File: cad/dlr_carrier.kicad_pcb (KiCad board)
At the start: 2 copper layers, 100 x 80 mm, 24 parts, among them J1 5V_IN, J2 CM4, J3 RS485, J4 USB_DEBUG, J5 I2C, J6 SPI, J7 GPIO, Q1 SI2301, U1 MAX3485, U2 CP2102N

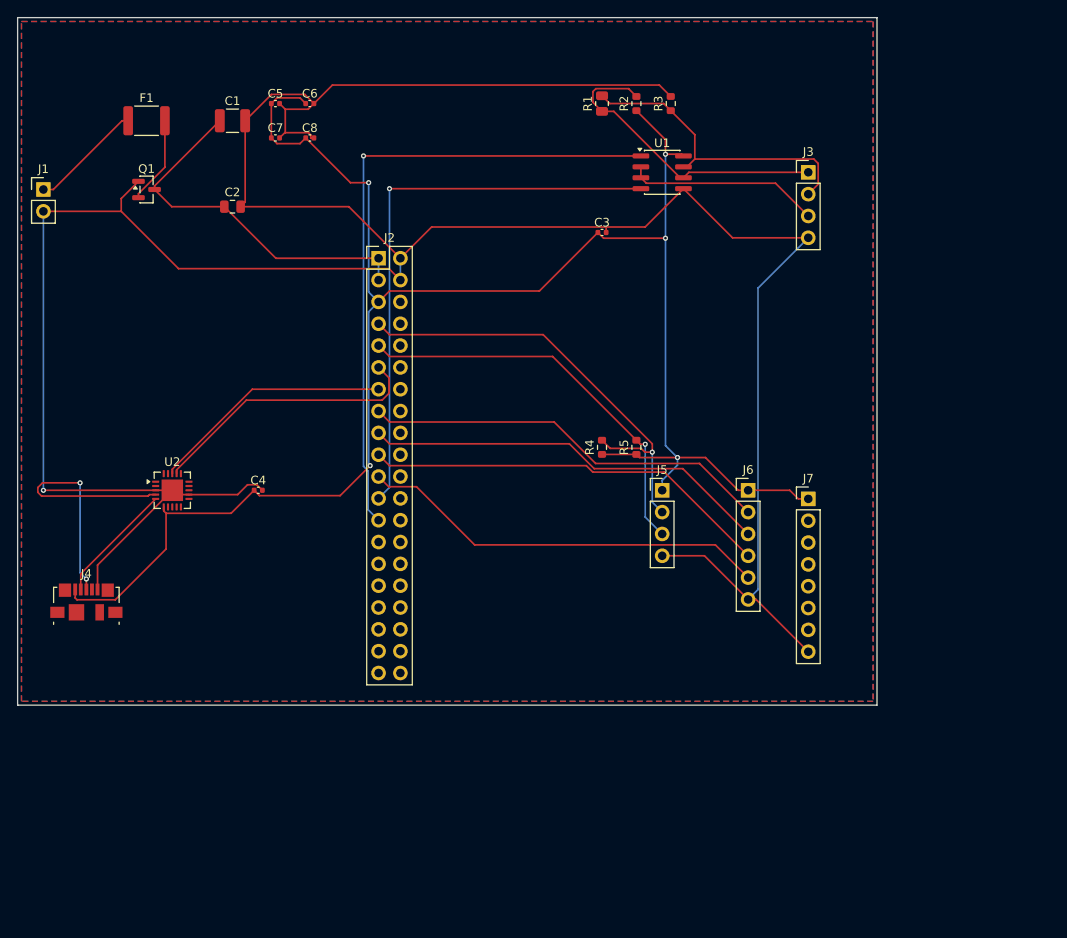
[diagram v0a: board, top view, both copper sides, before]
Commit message: 🔧 chore(cad): regenerate PCB layout, gerbers, and fab artifacts
Co-Authored-By: Claude Opus 4.7 (1M context) <noreply@anthropic.com>
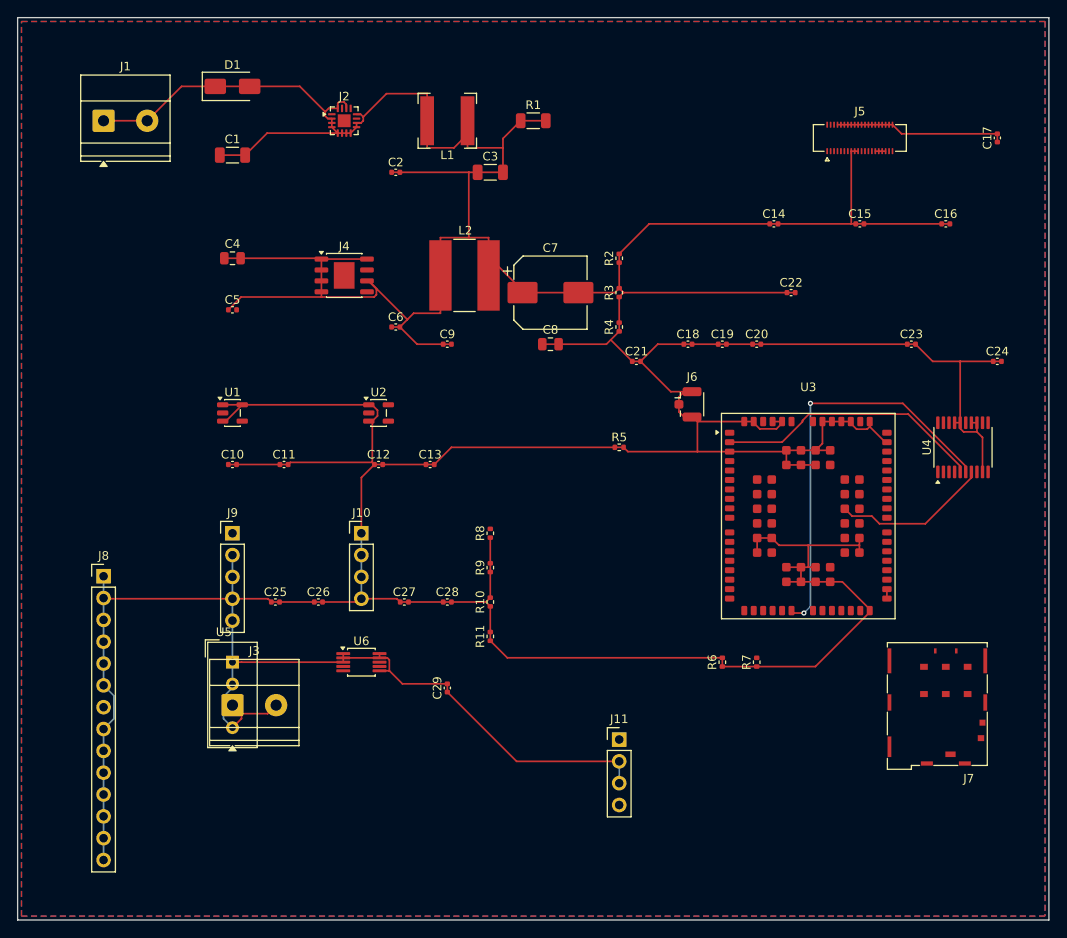
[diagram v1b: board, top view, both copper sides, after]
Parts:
- removed F1: 2A, Fuse:Fuse_1812_4532Metric
- removed Q1: SI2301, Package_TO_SOT_SMD:SOT-23
- added C10: 1uF, Capacitor_SMD:C_0402_1005Metric, F.Cu at (125.0, 132.0)
- added C11: 1uF, Capacitor_SMD:C_0402_1005Metric, F.Cu at (131.0, 132.0)
- added C12: 1uF, Capacitor_SMD:C_0402_1005Metric, F.Cu at (142.0, 132.0)
- added C13: 1uF, Capacitor_SMD:C_0402_1005Metric, F.Cu at (148.0, 132.0)
- added C14: 100nF, Capacitor_SMD:C_0402_1005Metric, F.Cu at (188.0, 104.0)
- added C15: 100nF, Capacitor_SMD:C_0402_1005Metric, F.Cu at (198.0, 104.0)
- added C16: 100nF, Capacitor_SMD:C_0402_1005Metric, F.Cu at (208.0, 104.0)
- added C17: 100nF, Capacitor_SMD:C_0402_1005Metric, F.Cu at (214.0, 94.0)
- added C18: 4.7uF, Capacitor_SMD:C_0402_1005Metric, F.Cu at (178.0, 118.0)
- added C19: 100nF, Capacitor_SMD:C_0402_1005Metric, F.Cu at (182.0, 118.0)
- added C20: 100nF, Capacitor_SMD:C_0402_1005Metric, F.Cu at (186.0, 118.0)
- added C21: DNP, Capacitor_SMD:C_0402_1005Metric, F.Cu at (172.0, 120.0)
- added C22: DNP, Capacitor_SMD:C_0402_1005Metric, F.Cu at (190.0, 112.0)
- added C23: 100nF, Capacitor_SMD:C_0402_1005Metric, F.Cu at (204.0, 118.0)
- added C24: 100nF, Capacitor_SMD:C_0402_1005Metric, F.Cu at (214.0, 120.0)
- added C25: 100nF, Capacitor_SMD:C_0402_1005Metric, F.Cu at (130.0, 148.0)
- added C26: 100nF, Capacitor_SMD:C_0402_1005Metric, F.Cu at (135.0, 148.0)
- added C27: 100nF, Capacitor_SMD:C_0402_1005Metric, F.Cu at (145.0, 148.0)
- added C28: 100nF, Capacitor_SMD:C_0402_1005Metric, F.Cu at (150.0, 148.0)
- added C29: 10nF, Capacitor_SMD:C_0402_1005Metric, F.Cu at (150.0, 158.0)
- added C9: 100nF, Capacitor_SMD:C_0402_1005Metric, F.Cu at (150.0, 118.0)
- added D1: SS34, Diode_SMD:D_SMA, F.Cu at (125.0, 88.0)
- added J10: YL-83, Connector_PinHeader_2.54mm:PinHeader_1x04_P2.54mm_Vertical, F.Cu at (140.0, 140.0)
- added J11: DEBUG_UART, Connector_PinHeader_2.54mm:PinHeader_1x04_P2.54mm_Vertical, F.Cu at (170.0, 164.0)
- added J8: FLIR_LEPTON, Connector_PinHeader_2.54mm:PinHeader_1x14_P2.54mm_Vertical, F.Cu at (110.0, 145.0)
- added J9: SI1145, Connector_PinHeader_2.54mm:PinHeader_1x05_P2.54mm_Vertical, F.Cu at (125.0, 140.0)
- added L1: 6.8uH, Inductor_SMD:L_Bourns-SRN6028, F.Cu at (150.0, 92.0)
- added L2: 10uH, Inductor_SMD:L_Bourns-SRN8040_8x8.15mm, F.Cu at (152.0, 110.0)
- added R10: 2.2k, Resistor_SMD:R_0402_1005Metric, F.Cu at (155.0, 148.0)
- added R11: 2.2k, Resistor_SMD:R_0402_1005Metric, F.Cu at (155.0, 152.0)
- added R6: 100k, Resistor_SMD:R_0402_1005Metric, F.Cu at (182.0, 155.0)
- added R7: 10k, Resistor_SMD:R_0402_1005Metric, F.Cu at (186.0, 155.0)
- added R8: 10k, Resistor_SMD:R_0402_1005Metric, F.Cu at (155.0, 140.0)
- added R9: 10k, Resistor_SMD:R_0402_1005Metric, F.Cu at (155.0, 144.0)
- added U3: BG770A-NA, RF_GSM:Quectel_BG95, F.Cu at (192.0, 138.0)
- added U4: TXS0108E, Package_SO:TSSOP-20_4.4x6.5mm_P0.65mm, F.Cu at (210.0, 130.0)
- added U5: DHT22, Sensor:Aosong_DHT11_5.5x12.0_P2.54mm, F.Cu at (125.0, 155.0)
- added U6: ADS1115, Package_SO:MSOP-10_3x3mm_P0.5mm, F.Cu at (140.0, 155.0)
- C1: value 100uF -> 22uF; footprint Capacitor_SMD:C_1210_3225Metric -> Capacitor_SMD:C_1206_3216Metric
- C2: value 10uF -> 100nF; footprint Capacitor_SMD:C_0805_2012Metric -> Capacitor_SMD:C_0402_1005Metric
- C3: value 100nF -> 22uF; footprint Capacitor_SMD:C_0402_1005Metric -> Capacitor_SMD:C_1206_3216Metric
- C4: value 100nF -> 4.7uF; footprint Capacitor_SMD:C_0402_1005Metric -> Capacitor_SMD:C_0805_2012Metric
- C7: value 100nF -> 470uF; footprint Capacitor_SMD:C_0402_1005Metric -> Capacitor_SMD:CP_Elec_8x10
- C8: value 100nF -> 22uF; footprint Capacitor_SMD:C_0402_1005Metric -> Capacitor_SMD:C_0805_2012Metric
- J1: value 5V_IN -> PV_IN; footprint Connector_PinHeader_2.54mm:PinHeader_1x02_P2.54mm_Vertical -> TerminalBlock_Phoenix:TerminalBlock_Phoenix_MKDS-1,5-2-5.08_1x02_P5.08mm_Horizontal
- J2: value CM4 -> BQ24650; footprint Connector_PinHeader_2.54mm:PinHeader_2x20_P2.54mm_Vertical -> Package_DFN_QFN:HVQFN-16-1EP_3x3mm_P0.5mm_EP1.5x1.5mm
- J3: value RS485 -> BAT; footprint Connector_PinHeader_2.54mm:PinHeader_1x04_P2.54mm_Vertical -> TerminalBlock_Phoenix:TerminalBlock_Phoenix_MKDS-1,5-2-5.08_1x02_P5.08mm_Horizontal
- J4: value USB_DEBUG -> LMR33630ADDA; footprint Connector_USB:USB_Micro-B_Molex_47346-0001 -> Package_SO:HSOP-8-1EP_3.9x4.9mm_P1.27mm_EP2.41x3.1mm
- J5: value I2C -> CM4_J2; footprint Connector_PinHeader_2.54mm:PinHeader_1x04_P2.54mm_Vertical -> Connector_Hirose_DF40:Hirose_DF40HC(3.0)-40DS-0.4V_2x20_P0.4mm
- J6: value SPI -> U.FL; footprint Connector_PinHeader_2.54mm:PinHeader_1x06_P2.54mm_Vertical -> Connector_Coaxial:U.FL_Hirose_U.FL-R-SMT-1_Vertical
- J7: value GPIO -> SIM; footprint Connector_PinHeader_2.54mm:PinHeader_1x08_P2.54mm_Vertical -> Connector_Card:microSIM_JAE_SF53S006VCBR2000
- R1: value 120 -> 20m; footprint Resistor_SMD:R_0805_2012Metric -> Resistor_SMD:R_1206_3216Metric
- R2: value 560 -> 39.2k; footprint Resistor_SMD:R_0603_1608Metric -> Resistor_SMD:R_0402_1005Metric
- R3: value 560 -> 10k; footprint Resistor_SMD:R_0603_1608Metric -> Resistor_SMD:R_0402_1005Metric
- R4: value 2.2k -> 47k; footprint Resistor_SMD:R_0603_1608Metric -> Resistor_SMD:R_0402_1005Metric
- R5: value 2.2k -> 0R; footprint Resistor_SMD:R_0603_1608Metric -> Resistor_SMD:R_0402_1005Metric
- U1: value MAX3485 -> AP2112K-3.3; footprint Package_SO:SOIC-8_3.9x4.9mm_P1.27mm -> Package_TO_SOT_SMD:SOT-23-5
- U2: value CP2102N -> LP5907MFX-3.8; footprint Package_DFN_QFN:QFN-20-1EP_4x4mm_P0.5mm_EP2.5x2.5mm -> Package_TO_SOT_SMD:SOT-23-5
- moved J3 91.3 mm to (125.0, 160.0)
- moved U1 57.3 mm to (125.0, 126.0)
- moved J4 48.4 mm to (138.0, 110.0)
- moved J5 47.0 mm to (198.0, 94.0)
- moved C8 36.9 mm to (162.0, 118.0)
- moved C7 36.7 mm to (162.0, 112.0)
- moved C6 27.9 mm to (144.0, 116.0)
- moved J7 27.2 mm to (208.0, 158.0)
- moved C4 27.2 mm to (125.0, 108.0)
- moved U2 25.6 mm to (142.0, 126.0)
- moved C5 24.5 mm to (125.0, 114.0)
- moved R3 22.8 mm to (170.0, 112.0)
- moved C2 19.4 mm to (144.0, 98.0)
- moved R2 18.1 mm to (170.0, 108.0)
- moved J2 16.5 mm to (138.0, 92.0)
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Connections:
- C1 pad 1: +5V -> +3V3
- C1 pad 2: GND -> +3V3
- C2 pad 1: +5V -> +3V3
- C2 pad 2: GND -> +3V3
- C3 pad 2: GND -> +3V3
- C4 pad 2: GND -> +3V3
- C6 pad 2: GND -> +3V3
- C7 pad 2: GND -> +3V3
- C8 pad 2: GND -> +3V3
- J1 pad 1: /5V_IN -> +3V3
- J1 pad 2: GND -> +3V3
- J2 pad 1: +5V -> unconnected-(J2-Pin_1-Pad1)
- J2 pad 10: unconnected-(J2-Pin_10-Pad10) -> +3V3
- J2 pad 11: /UART_TX -> unconnected-(J2-Pin_11-Pad11)
- J2 pad 12: unconnected-(J2-Pin_12-Pad12) -> +3V3
- J2 pad 13: /UART_RX -> unconnected-(J2-Pin_13-Pad13)
- J2 pad 14: unconnected-(J2-Pin_14-Pad14) -> +3V3
- J2 pad 15: /MOSI -> unconnected-(J2-Pin_15-Pad15)
- J2 pad 16: unconnected-(J2-Pin_16-Pad16) -> +3V3
- J2 pad 17: /MISO -> (no net)
- J2 pad 2: GND -> +3V3
- J2 pad 3: +5V -> +3V3
- J2 pad 4: GND -> +3V3
- J2 pad 6: unconnected-(J2-Pin_6-Pad6) -> +3V3
- J2 pad 7: /SDA -> +3V3
- J2 pad 8: unconnected-(J2-Pin_8-Pad8) -> +3V3
- J2 pad 9: /SCL -> +3V3
- J3 pad 1: /RS485_A -> +3V3
- J3 pad 2: /RS485_B -> +3V3
- J4 pad 2: /USB_DM -> +3V3
- J4 pad 3: /USB_DP -> +3V3
- J4 pad 4: unconnected-(J4-ID-Pad4) -> +3V3
- J4 pad 5: GND -> unconnected-(J4-Pin_5-Pad5)
- J4 pad 6: unconnected-(J4-Shield-Pad6)_3 -> +3V3
- J5 pad 2: /SDA -> unconnected-(J5-Pin_2-Pad2)
- J5 pad 3: /SCL -> +3V3
- J5 pad 4: GND -> unconnected-(J5-Pin_4-Pad4)
- J6 pad 2: /MOSI -> +3V3
- R1 pad 1: /RS485_A -> +3V3
- R1 pad 2: /RS485_B -> +3V3
- R2 pad 2: /RS485_A -> +3V3
- R3 pad 1: /RS485_B -> +3V3
- R3 pad 2: GND -> +3V3
- R4 pad 2: /SDA -> +3V3
- R5 pad 2: /SCL -> +3V3
- U1 pad 1: /RS485_RX -> +3V3
- U1 pad 2: /RS485_DE -> unconnected-(U1-GND-Pad2)
- U1 pad 3: /RS485_DE -> +3V3
- U1 pad 4: /RS485_TX -> unconnected-(U1-NC-Pad4)
- U1 pad 5: GND -> +3V3
- U2 pad 1: unconnected-(U2-RS485/GPIO.1-Pad1) -> +3V3
- U2 pad 3: GND -> +3V3
- U2 pad 4: /USB_DP -> unconnected-(U2-NC-Pad4)
- U2 pad 5: /USB_DM -> unconnected-(U2-OUT-Pad5)
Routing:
- net +3V3: track 214.4 -> 806.4 mm, vias 5 -> 0
- net GND: track 342.3 -> 0.00 mm, vias 1 -> 0
- net /RS485_RX: track 75.4 -> 0.00 mm, vias 1 -> 0
- net /RS485_TX: track 65.8 -> 0.00 mm, vias 1 -> 0
- net /SDA: track 52.5 -> 0.00 mm, vias 1 -> 0
- net /CELL_PWRKEY_1V8: track 0.00 -> 48.0 mm, vias 0 -> 2
- net /SCK: track 47.9 -> 0.00 mm
- net /MISO: track 47.9 -> 0.00 mm
- net /MOSI: track 47.9 -> 0.00 mm
- net /SPI_CS0: track 47.9 -> 0.00 mm
- net /SCL: track 47.0 -> 0.00 mm, vias 1 -> 0
- net +5V: track 43.1 -> 0.00 mm
- net /RS485_B: track 35.8 -> 0.00 mm
- net /RS485_A: track 35.8 -> 0.00 mm
- net /USB_DP: track 32.4 -> 0.00 mm, vias 2 -> 0
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- added copper zone on F.Cu, net +3V3
- removed copper zone on F.Cu, net GND
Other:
- board size 100 x 80 mm -> 120 x 105 mm
